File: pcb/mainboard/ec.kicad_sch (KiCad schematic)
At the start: 28 parts, among them J301 Conn_01x06_MountingPin, U301 LPC5500_FBD64, U302 74LS154, Y301 16MHz

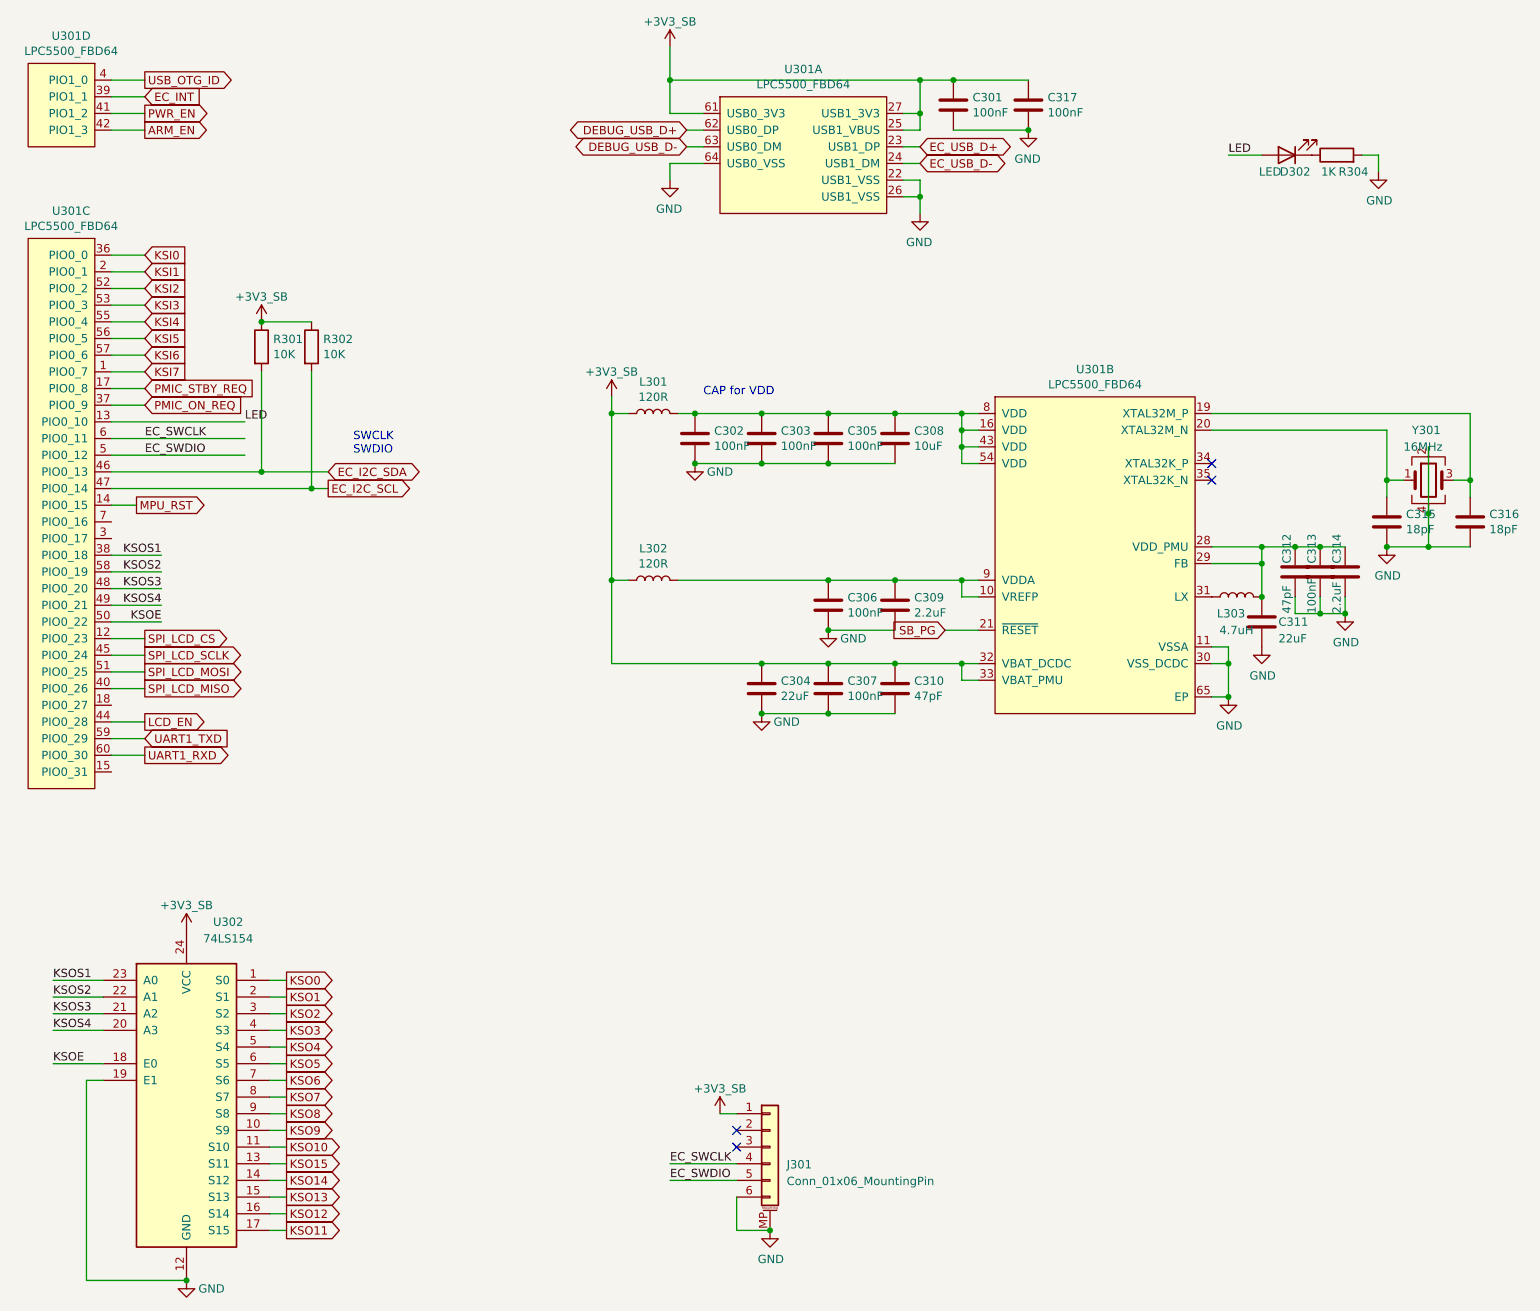
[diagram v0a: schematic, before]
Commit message: pcb: preliminary r0p1 schematics
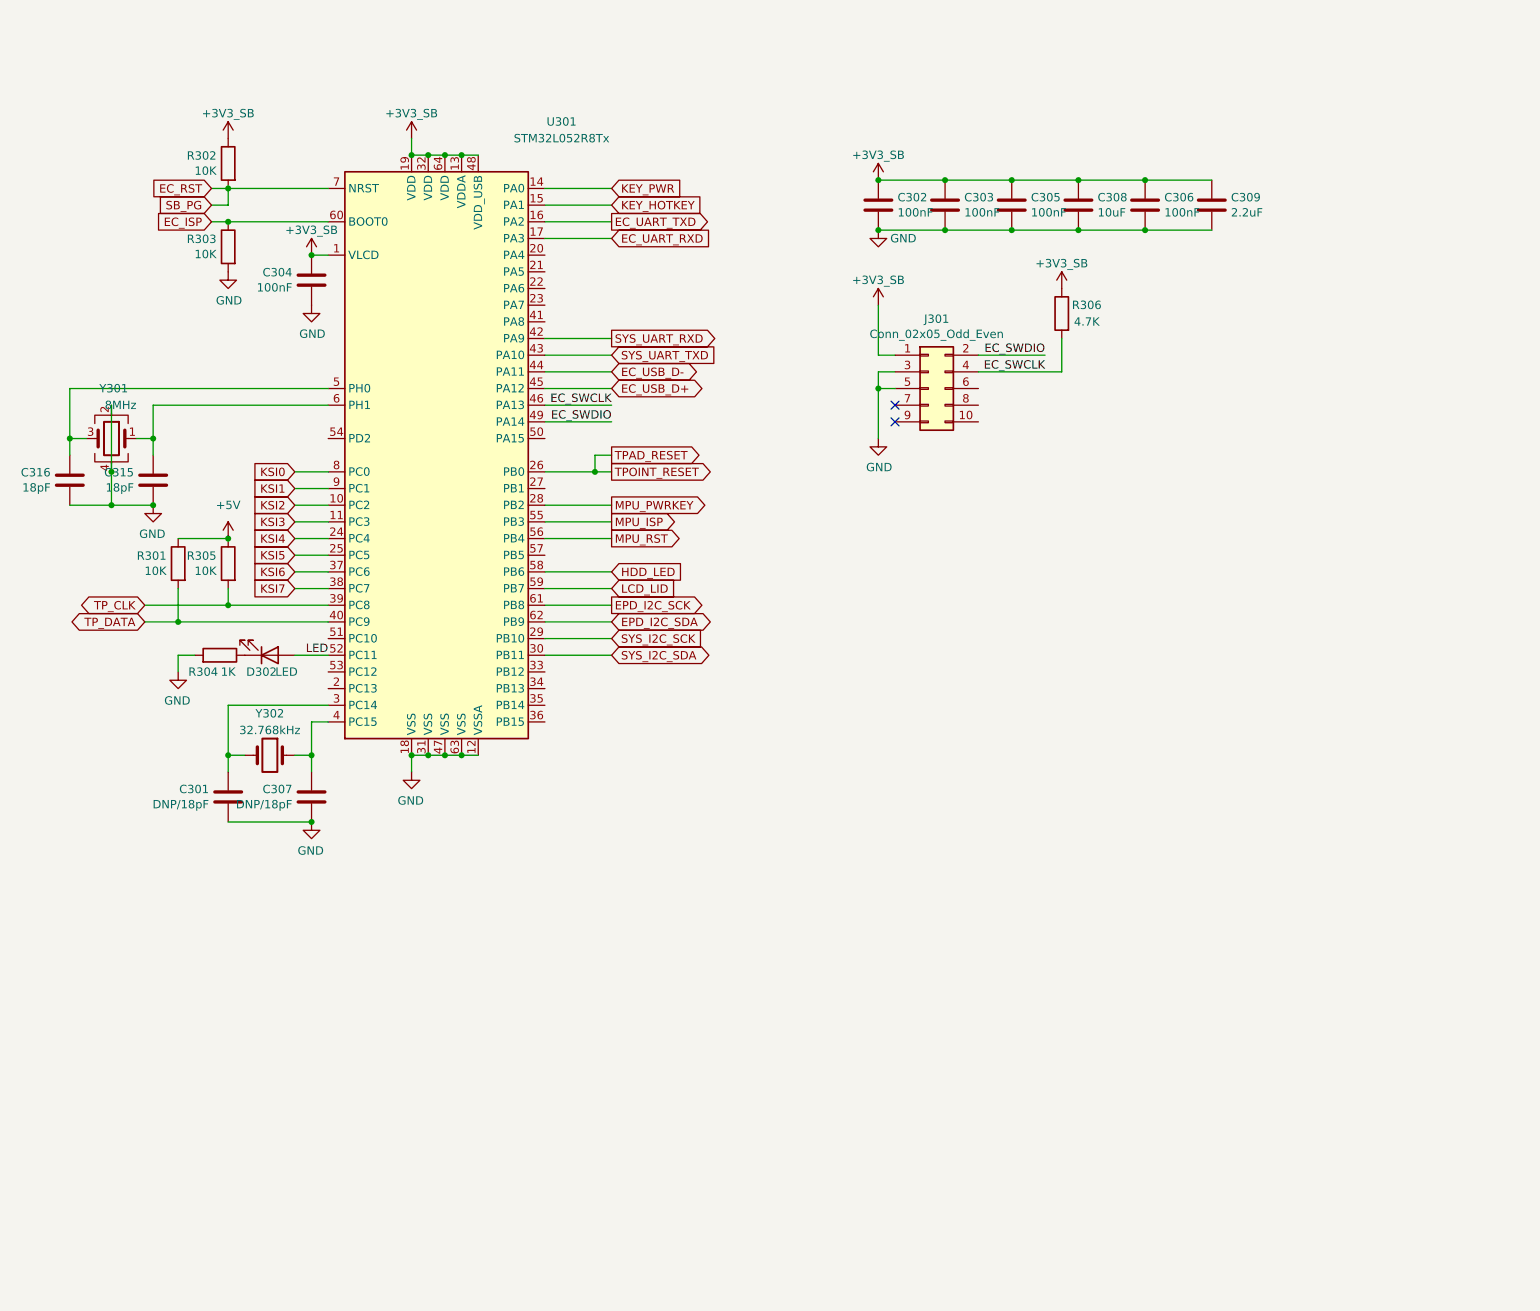
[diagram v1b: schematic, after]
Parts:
- removed C310, C312: 47pF, Capacitor_SMD:C_0402_1005Metric, symbol Device:C
- removed C311: 22uF, Capacitor_SMD:C_0603_1608Metric, symbol Device:C
- removed C313, C317: 100nF, Capacitor_SMD:C_0402_1005Metric, symbol Device:C
- removed C314: 2.2uF, Capacitor_SMD:C_0402_1005Metric, symbol Device:C
- removed J301: Conn_01x06_MountingPin, Connector_FFC-FPC:Hirose_FH12-6S-0.5SH_1x06-1MP_P0.50mm_Horizontal, symbol Connector_Generic_MountingPin:Conn_01x06_MountingPin
- removed L301, L302: 120R, Inductor_SMD:L_0603_1608Metric, symbol Device:L
- removed L303: 4.7uH, Inductor_SMD:L_Vishay_IHLP-1212, symbol Device:L
- removed U301: LPC5500_FBD64, Package_QFP:LQFP-64-1EP_10x10mm_P0.5mm_EP5x5mm_ThermalVias, symbol symbols:LPC5500_FBD64
- removed U302: 74LS154, Package_SO:SO-24_5.3x15mm_P1.27mm, symbol 74xx:74LS154
- added J301: Conn_02x05_Odd_Even, Connector_PinHeader_1.27mm:PinHeader_2x05_P1.27mm_Vertical_SMD, symbol Connector_Generic:Conn_02x05_Odd_Even
- added R303, R305: 10K, Resistor_SMD:R_0402_1005Metric, symbol Device:R
- added R306: 4.7K, Resistor_SMD:R_0402_1005Metric, symbol Device:R
- added U301: STM32L052R8Tx, Package_QFP:LQFP-64_10x10mm_P0.5mm, symbol MCU_ST_STM32L0:STM32L052R8Tx
- added Y302: 32.768kHz, Crystal:Crystal_SMD_TXC_9HT11-2Pin_2.0x1.2mm_HandSoldering, symbol Device:Crystal
- C301, C307: value 100nF -> DNP/18pF
- C304: value 22uF -> 100nF; footprint Capacitor_SMD:C_0603_1608Metric -> Capacitor_SMD:C_0402_1005Metric
- Y301: value 16MHz -> 8MHz
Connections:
- net +3V3_SB: now also C302.1, C303.1, C305.1, C306.1, C308.1, C309.1, J301.1 (Pin_1), R306.1, U301.1 (VLCD), U301.13 (VDDA), U301.19 (VDD), U301.32 (VDD), U301.48 (VDD_USB), U301.64 (VDD); no longer C301.1, C307.1, R301.1
- net EC_SWCLK: now also J301.4 (Pin_4), R306.2, U301.46 (PA13)
- net EC_SWDIO: now also J301.2 (Pin_2), U301.49 (PA14)
- net EC_USB_D+: now also U301.45 (PA12)
- net EC_USB_D-: now also U301.44 (PA11)
- net GND: now also J301.3 (Pin_3), J301.5 (Pin_5), R303.2, U301.12 (VSSA), U301.18 (VSS), U301.31 (VSS), U301.47 (VSS), U301.63 (VSS)
- net KSI0: now also U301.8 (PC0)
- net KSI1: now also U301.9 (PC1)
- net KSI2: now also U301.10 (PC2)
- net KSI3: now also U301.11 (PC3)
- net KSI4: now also U301.24 (PC4)
- net KSI5: now also U301.25 (PC5)
- net KSI6: now also U301.37 (PC6)
- net KSI7: now also U301.38 (PC7)
- net LED: now also U301.52 (PC11)
- net MPU_RST: now also U301.56 (PB4)
- net at C316.1, Y301.3: now also U301.5 (PH0)
- net at C315.1, Y301.1: now also U301.6 (PH1)
- net EC_I2C_SCL renamed EC_RST
- net EC_RST: now also U301.7 (NRST)
- net EC_I2C_SDA renamed TP_DATA
- net TP_DATA: now also U301.40 (PC9)
- new net: C301.1, U301.3 (PC14), Y302.2
- new net: C307.1, U301.4 (PC15), Y302.1
- new net +5V: R301.1, R305.1
- new net EC_ISP: R303.1, U301.60 (BOOT0)
- new net EC_UART_RXD: U301.17 (PA3)
- new net EC_UART_TXD: U301.16 (PA2)
- new net EPD_I2C_SCK: U301.61 (PB8)
- new net EPD_I2C_SDA: U301.62 (PB9)
- new net HDD_LED: U301.58 (PB6)
- new net KEY_HOTKEY: U301.15 (PA1)
- new net KEY_PWR: U301.14 (PA0)
- new net LCD_LID: U301.59 (PB7)
- new net MPU_ISP: U301.55 (PB3)
- new net MPU_PWRKEY: U301.28 (PB2)
- new net SYS_I2C_SCK: U301.29 (PB10)
- new net SYS_I2C_SDA: U301.30 (PB11)
- new net SYS_UART_RXD: U301.42 (PA9)
- new net SYS_UART_TXD: U301.43 (PA10)
- new net TPAD_RESET: U301.26 (PB0)
- new net TP_CLK: R305.2, U301.39 (PC8)
- no-connect marks 4 -> 2
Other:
- note removed: "CAP for VDD"
- note removed: "SWCLK SWDIO"
- company: Copyright EI-2030 2021. / Engineer: Wenting Zhang -> Copyright Modos 2021. / Engineer: Wenting Zhang
- moved on the sheet: C302, C303, C305, C306, C308, C309, C315, C316, D302, R304, Y301

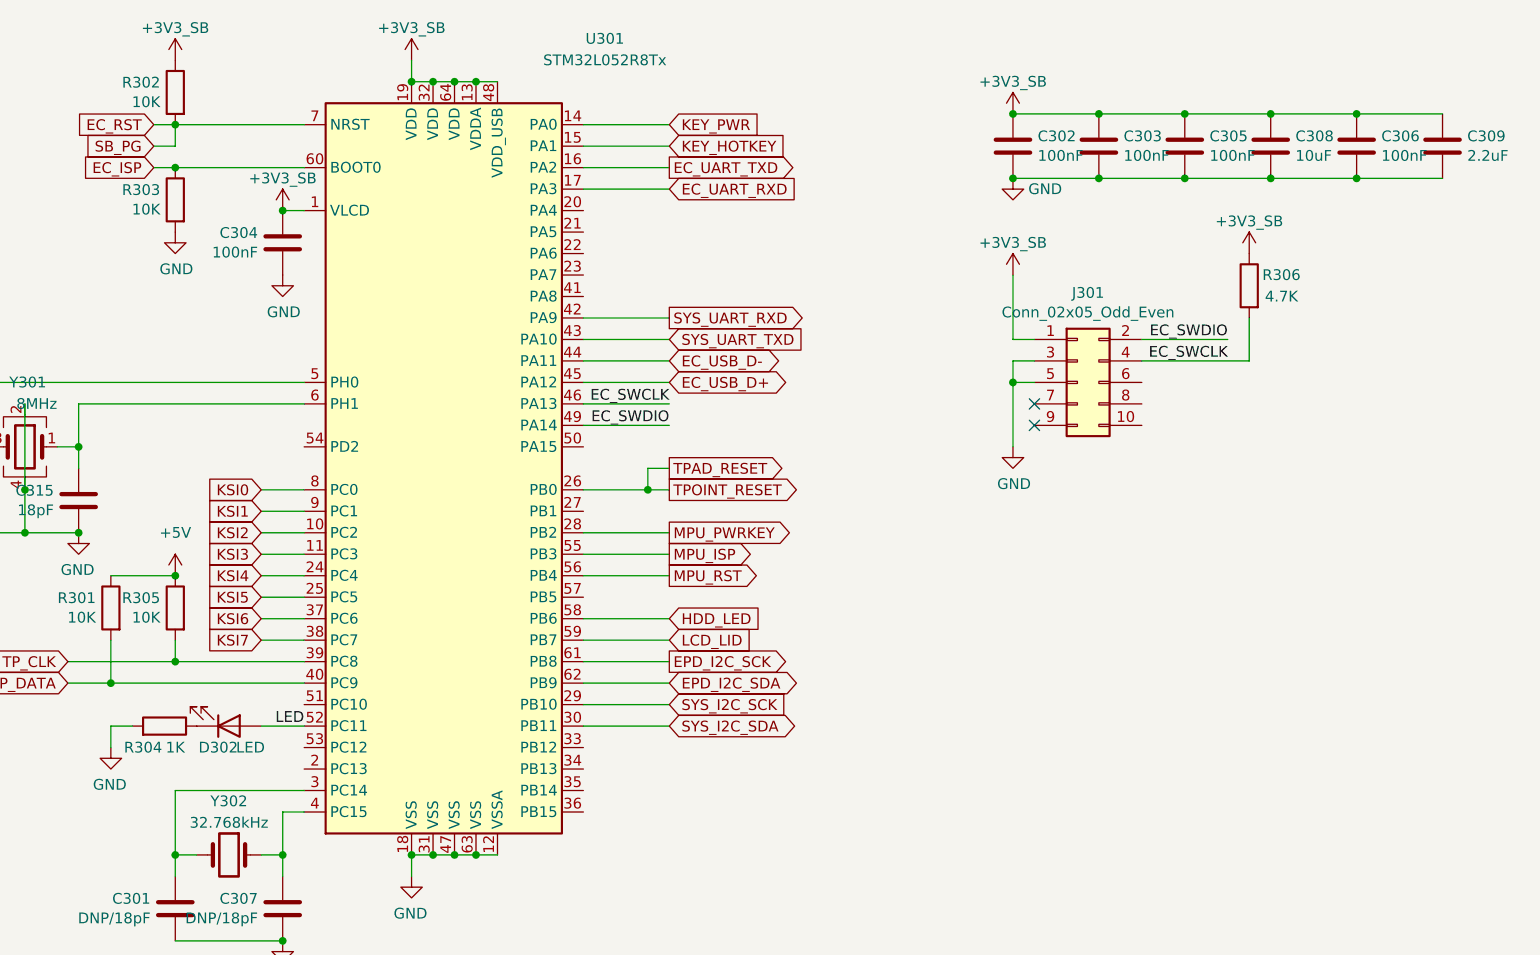
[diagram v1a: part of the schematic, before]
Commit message: pcb: initial placement for mb
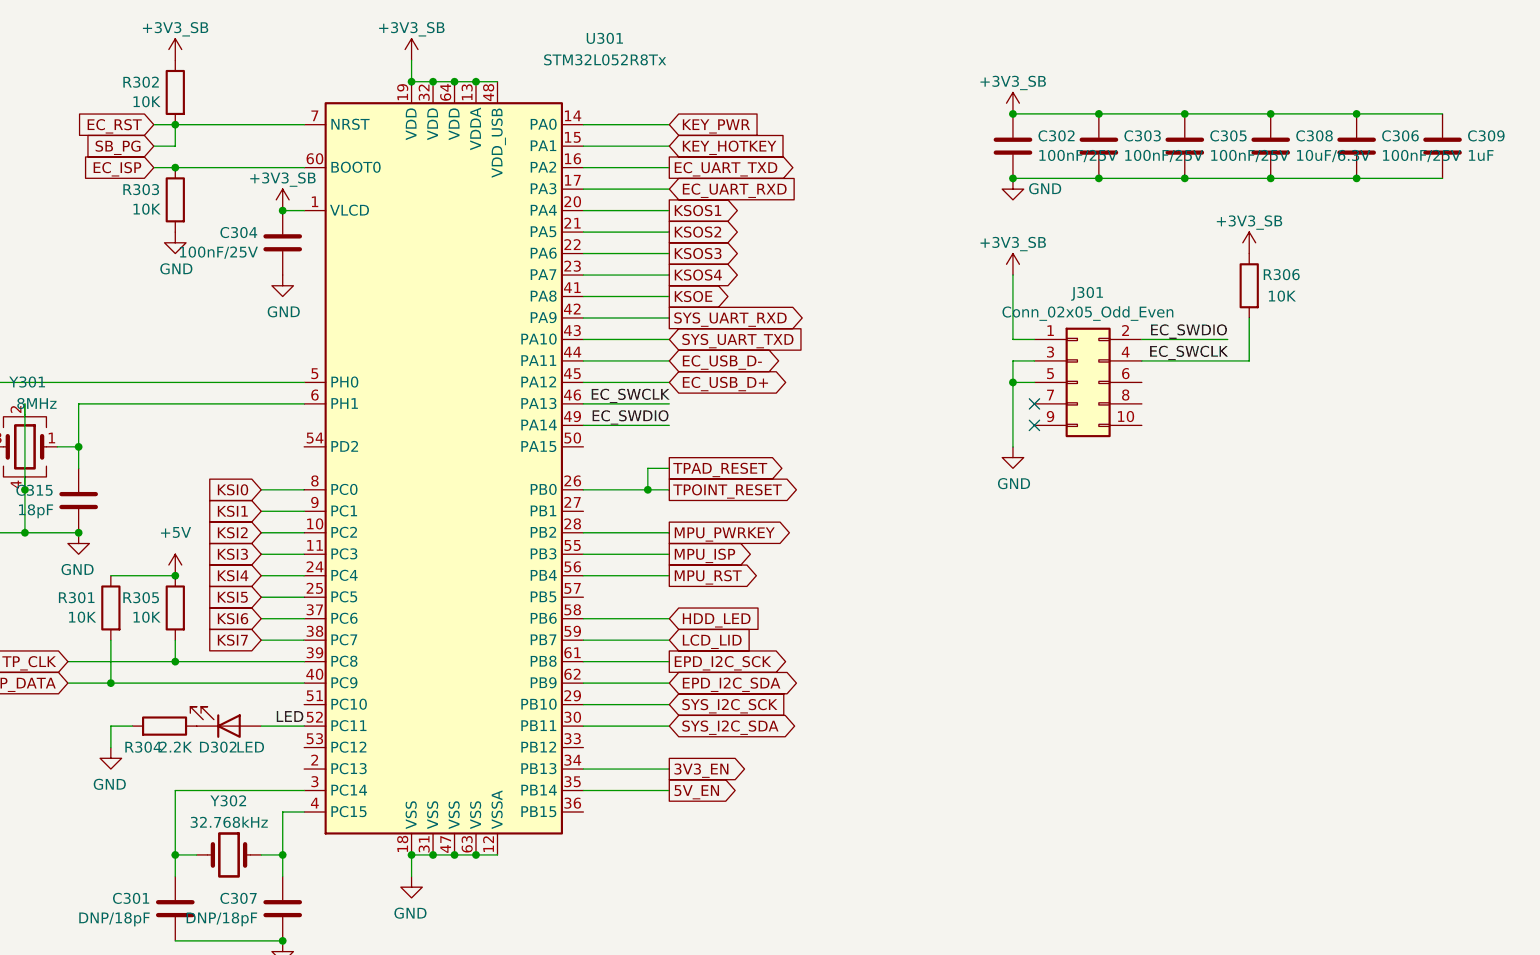
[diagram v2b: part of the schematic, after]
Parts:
- C301, C307: LCSC (none) -> -; Ref.Price (none) -> 0
- C302, C303, C304, C305, C306: value 100nF -> 100nF/25V; LCSC (none) -> C56392; Ref.Price (none) -> 0.0023
- C308: value 10uF -> 10uF/6.3V; LCSC (none) -> C105490; Ref.Price (none) -> 0.0165
- C309: value 2.2uF -> 1uF; LCSC (none) -> C157353; Ref.Price (none) -> 0.0034
- C315, C316: LCSC (none) -> C182481; Ref.Price (none) -> 0.0061
- D302: LCSC (none) -> C90692; Ref.Price (none) -> 0.0176
- J301: LCSC (none) -> C150517; Ref.Price (none) -> 0.5212
- R301, R302, R303, R305: LCSC (none) -> C60489; Ref.Price (none) -> 0.0006
- R304: value 1K -> 2.2K; LCSC (none) -> C163447; Ref.Price (none) -> 0.0007
- R306: value 4.7K -> 10K; LCSC (none) -> C60489; Ref.Price (none) -> 0.0006
- U301: LCSC (none) -> C139720; Ref.Price (none) -> 2.2253
- Y301: footprint Oscillator:Oscillator_SMD_Abracon_ASE-4Pin_3.2x2.5mm -> Crystal:Crystal_SMD_3225-4Pin_3.2x2.5mm; LCSC (none) -> C479192; Ref.Price (none) -> 0.1913
- Y302: LCSC (none) -> C99009; Ref.Price (none) -> 0.3337
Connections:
- net KSOS1: now reaches U301.20 (PA4)
- net KSOS2: now reaches U301.21 (PA5)
- net KSOS3: now reaches U301.22 (PA6)
- net KSOS4: now reaches U301.23 (PA7)
- net 3V3_EN: now reaches U301.34 (PB13)
- net 5V_EN: now reaches U301.35 (PB14)
- net KSOE: now reaches U301.41 (PA8)
